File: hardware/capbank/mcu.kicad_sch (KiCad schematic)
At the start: 19 parts, among them J1 Conn_01x03_Socket, J3 Conn_01x02, J4 Conn_01x02, J6 Conn_01x05, J7 Conn_01x06, SW2 SW_SPST, SW3 SW_DIP_x01, SW4 SW_DIP_x04, U6 ATtiny84A-P, U8 M24C16-RMN6TP

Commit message: Blinky!
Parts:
- removed J1: Conn_01x03_Socket, Connector_PinHeader_2.54mm:PinHeader_1x03_P2.54mm_Vertical, symbol Connector:Conn_01x03_Socket
- removed J6: Conn_01x05, Connector_PinHeader_2.54mm:PinHeader_1x05_P2.54mm_Vertical, symbol Connector_Generic:Conn_01x05
- added J5: Conn_01x06, symbol Connector_Generic:Conn_01x06
- added Y1: 16MHz, symbol Device:Resonator
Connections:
- net GND: now also J5.1 (Pin_1), Y1.2
- net PRG_MISO_SPI_CS: now also J5.4 (Pin_4)
- net PRG_MOSI_I2C_SDA: now also J5.3 (Pin_3)
- net PRG_SCK_I2C_SCL: now also J5.5 (Pin_5)
- net VDD: now also J5.6 (Pin_6)
- net XTAL1: now also Y1.1
- net XTAL2: now also Y1.3
- net ~{RESET}: now also R8.2, SW2.2 (B), J5.2 (Pin_2)
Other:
- note removed: "HVSP toggles Allows connecting ~{RESET} to 12V, or to the normal RESET circuitry"

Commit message: KiCad changes
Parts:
- removed C36: 100n, PCM_Capacitor_SMD_AKL:C_0603_1608Metric, symbol Device:C
- removed SW3: SW_DIP_x01, Button_Switch_THT:SW_DIP_SPSTx01_Slide_9.78x4.72mm_W7.62mm_P2.54mm, symbol Switch:SW_DIP_x01
- removed U8: M24C16-RMN6TP, Package_SO:SOIC-8_3.9x4.9mm_P1.27mm, symbol eeprom:M24C16-RMN6TP
- added D8: LED, PCM_Diode_SMD_Handsoldering_AKL:D_0603_1608Metric, symbol Device:LED
- added R4: 1k, PCM_Resistor_SMD_AKL:R_0603_1608Metric, symbol Device:R
- added TP23: ~, TestPoint:TestPoint_THTPad_1.5x1.5mm_Drill0.7mm, symbol Connector:TestPoint
- J5: footprint (none) -> Connector_PinHeader_2.54mm:PinHeader_1x06_P2.54mm_Vertical
- Y1: footprint (none) -> Crystal:Resonator-3Pin_W7.0mm_H2.5mm
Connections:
- net GND: now also D8.1 (K)
- net PRG_MOSI_I2C_SDA renamed PRG_MOSI_LED
- net PRG_MOSI_LED: now also R4.1
- net PRG_SCK_I2C_SCL renamed PRG_SCK_FREE
- net PRG_SCK_FREE: now also TP23.1
- new net: D8.2 (A), R4.2
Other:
- moved on the sheet: C35, C37, U6

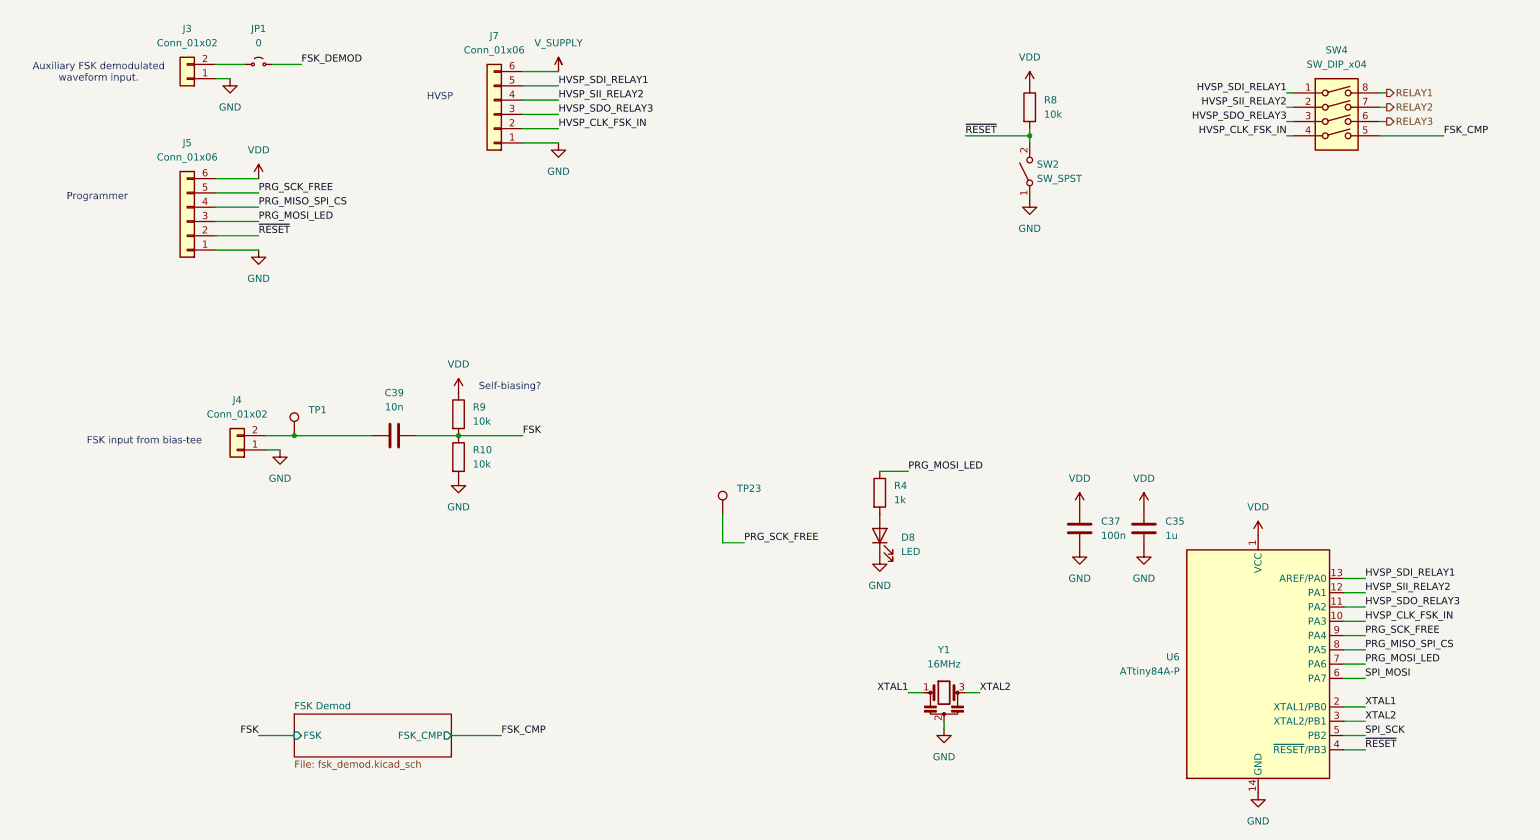
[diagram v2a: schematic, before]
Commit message: Progress, layout nearly completed, build oscillator on breadboard
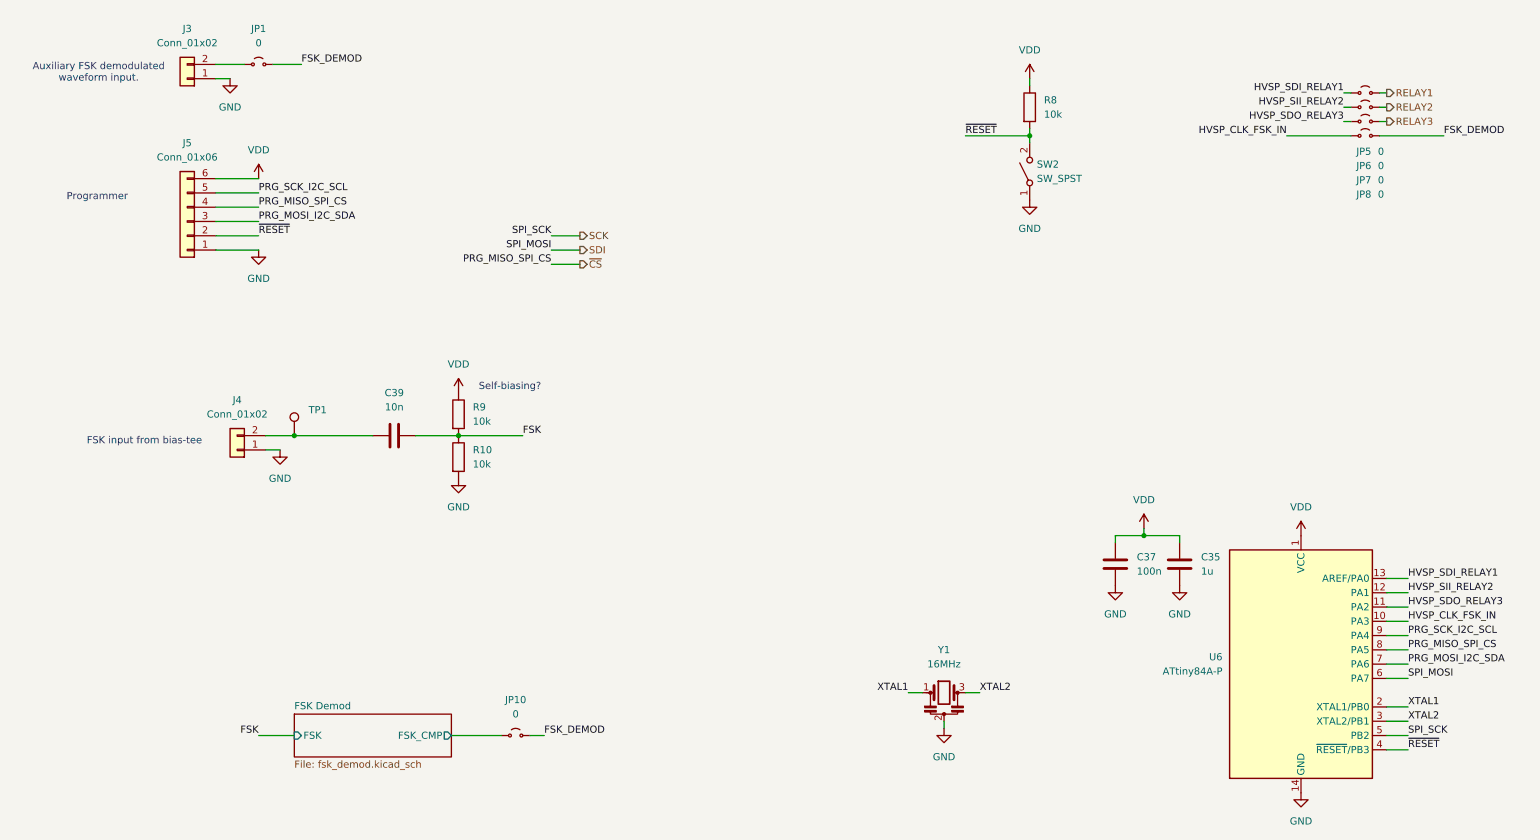
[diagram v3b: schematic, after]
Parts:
- removed D8: LED, PCM_Diode_SMD_Handsoldering_AKL:D_0603_1608Metric, symbol Device:LED
- removed J7: Conn_01x06, Connector_PinHeader_2.54mm:PinHeader_1x06_P2.54mm_Vertical, symbol Connector_Generic:Conn_01x06
- removed R4: 1k, PCM_Resistor_SMD_AKL:R_0603_1608Metric, symbol Device:R
- removed SW4: SW_DIP_x04, Button_Switch_SMD:SW_DIP_SPSTx04_Slide_9.78x12.34mm_W8.61mm_P2.54mm, symbol Switch:SW_DIP_x04
- removed TP23: ~, TestPoint:TestPoint_THTPad_1.5x1.5mm_Drill0.7mm, symbol Connector:TestPoint
- added JP10, JP5, JP6, JP7, JP8: 0, PCM_Resistor_SMD_AKL:R_0603_1608Metric, symbol Jumper:Jumper_2_Small_Open
- J5: footprint Connector_PinHeader_2.54mm:PinHeader_1x06_P2.54mm_Vertical -> (none)
- SW2: footprint Button_Switch_THT:SW_PUSH_6mm -> Button_Switch_SMD:SW_SPST_CK_KXT3
- Y1: footprint Crystal:Resonator-3Pin_W7.0mm_H2.5mm -> (none)
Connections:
- net FSK_DEMOD: now also JP10.2 (B), JP8.2 (B)
- net HVSP_CLK_FSK_IN: now also JP8.1 (A)
- net HVSP_SDI_RELAY1: now also JP5.1 (A)
- net HVSP_SDO_RELAY3: now also JP7.1 (A)
- net HVSP_SII_RELAY2: now also JP6.1 (A)
- net RELAY1: now also JP5.2 (B)
- net RELAY2: now also JP6.2 (B)
- net RELAY3: now also JP7.2 (B)
- net PRG_MISO_SPI_CS renamed ~{CS}
- net PRG_MOSI_LED renamed PRG_MOSI_I2C_SDA
- net PRG_SCK_FREE renamed PRG_SCK_I2C_SCL
- net SPI_MOSI renamed SDI
- net SPI_SCK renamed SCK
- new net FSK Demod/FSK_CMP: JP10.1 (A)
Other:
- note removed: "HVSP"
- moved on the sheet: C35, C37, U6
